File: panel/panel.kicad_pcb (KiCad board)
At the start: 4 copper layers, 36 x 36 mm, 288 parts, among them J1 IN, J2 OUT, Q1 Q_PMOS_GSD, Q10 Q_PMOS_GSD, Q11 Q_PMOS_GSD, Q12 Q_PMOS_GSD, Q13 Q_PMOS_GSD, Q14 Q_PMOS_GSD, Q15 Q_PMOS_GSD, Q16 Q_PMOS_GSD, Q2 Q_PMOS_GSD, Q3 Q_PMOS_GSD, Q4 Q_PMOS_GSD, Q5 Q_PMOS_GSD, Q6 Q_PMOS_GSD, Q7 Q_PMOS_GSD, Q8 Q_PMOS_GSD, Q9 Q_PMOS_GSD, U1 TLC59025, U2 TLC59025, U3 TLC59025, U4 SN74HC595, U5 SN74HC595, U6 NC7WZ17, U7 NC7WZ17

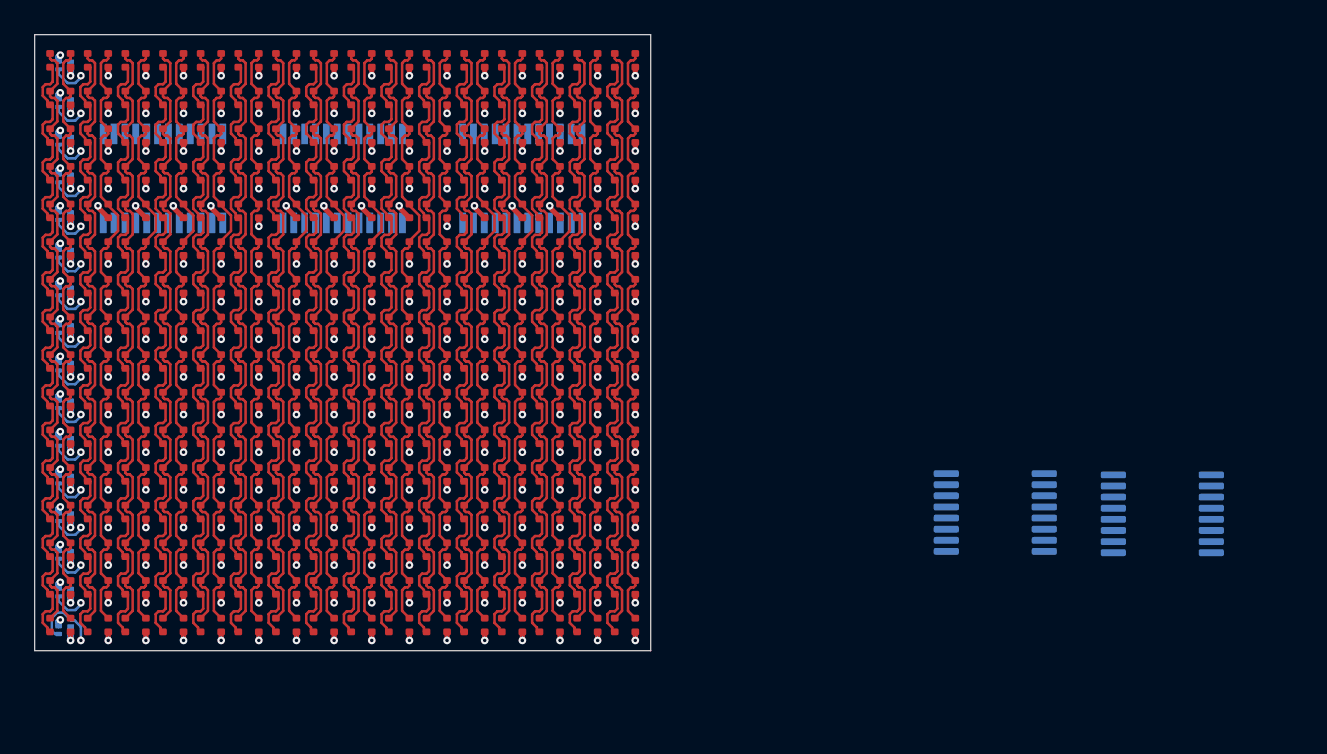
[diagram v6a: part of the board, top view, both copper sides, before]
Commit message: VCC plane and row driver placement
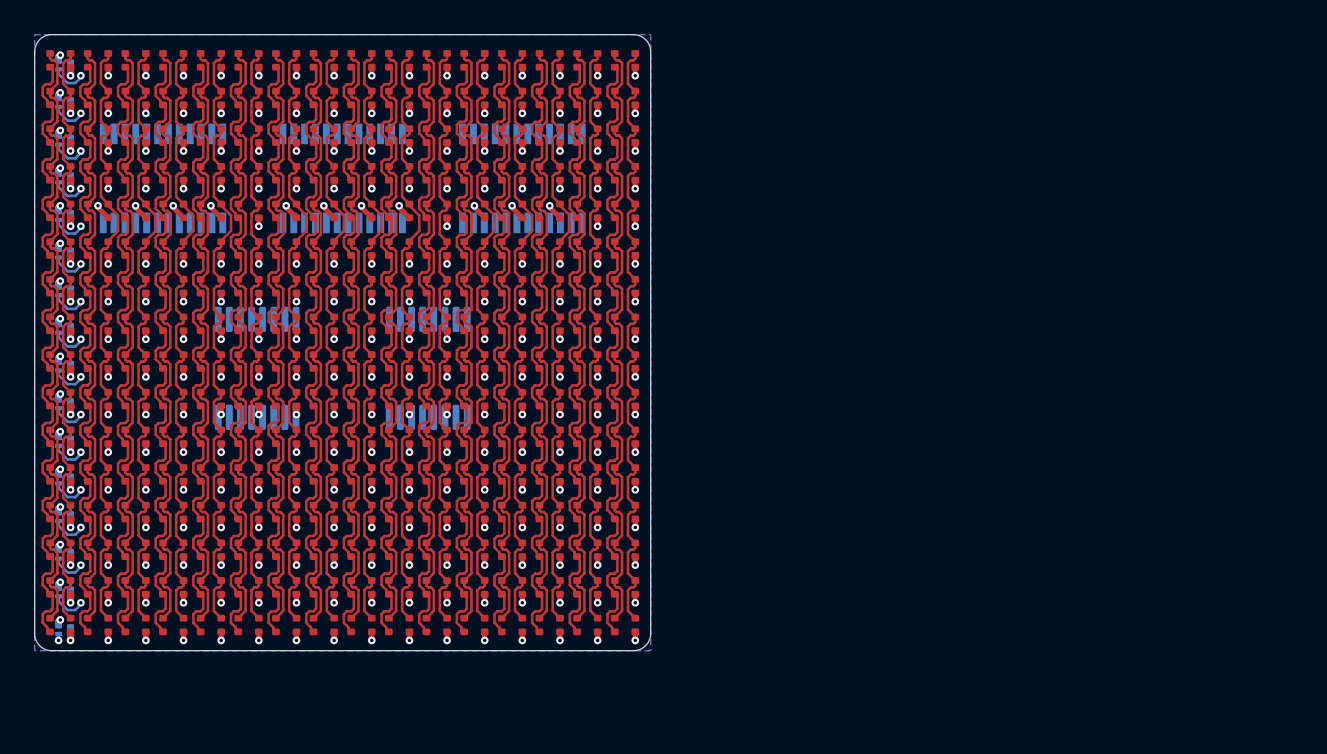
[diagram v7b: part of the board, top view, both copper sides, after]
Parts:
- moved U4 44.0 mm to (73.0, 79.5), turned to 90 degrees
- moved U5 43.7 mm to (83.0, 79.5), turned to -90 degrees
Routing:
- net /ROW_15: track 4.19 -> 0.38 mm
- added copper zone on B.Cu, net GND
- added copper zone on In2.Cu, net VCC
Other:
- outline, holes or cut-outs redrawn

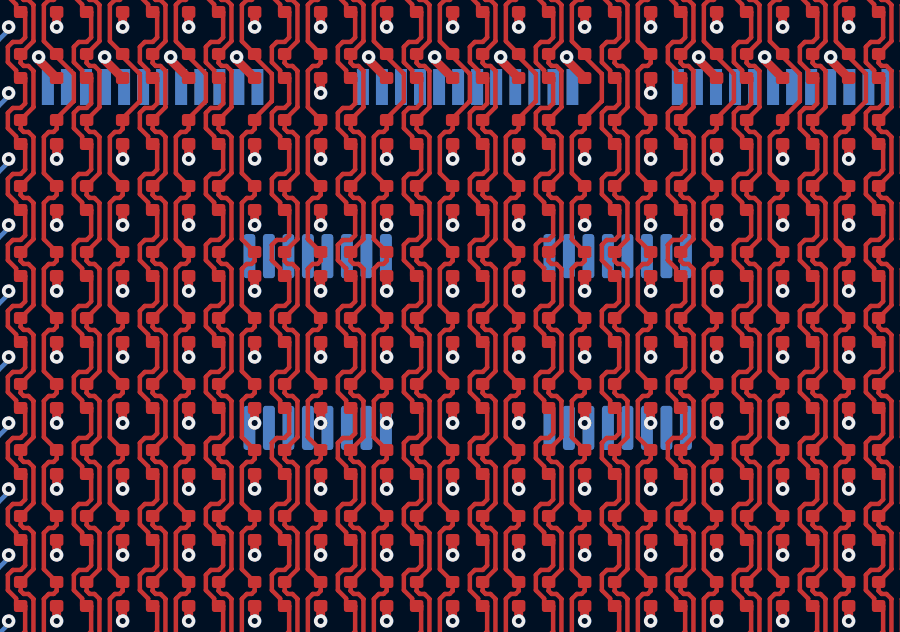
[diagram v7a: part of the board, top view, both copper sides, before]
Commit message: Routed rows around row driver pins
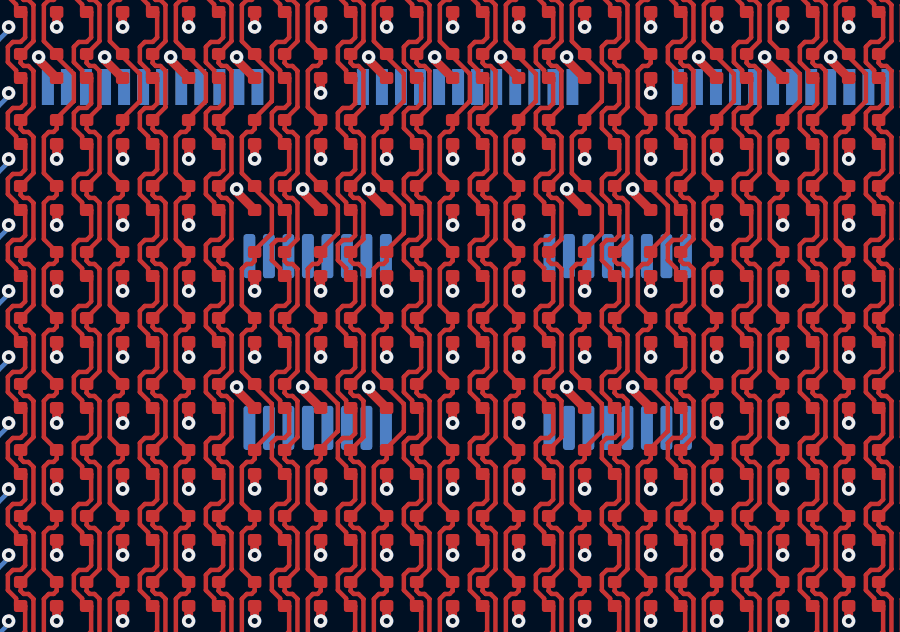
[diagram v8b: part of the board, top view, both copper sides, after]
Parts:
- added D102: LED_RABG, panel:MHPA1515RGBDT, F.Cu at (72.5, 74.7)
